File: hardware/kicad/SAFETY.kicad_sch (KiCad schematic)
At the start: 0 parts

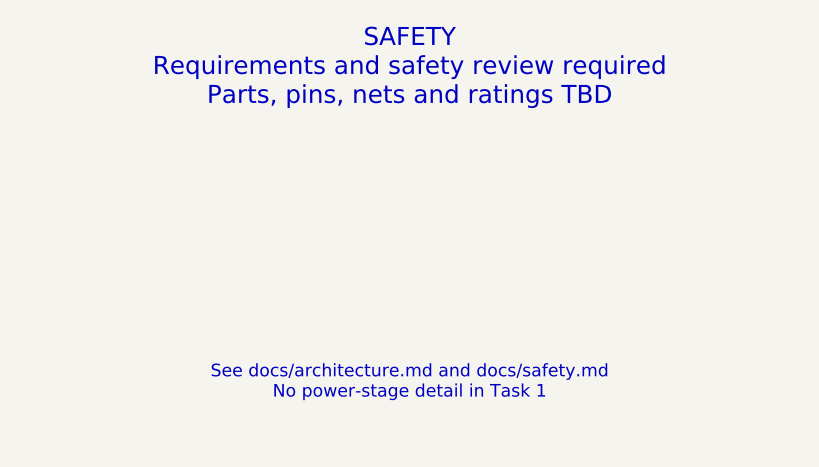
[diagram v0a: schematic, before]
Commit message: hardware: update existing KiCad architecture and add precharge sheet
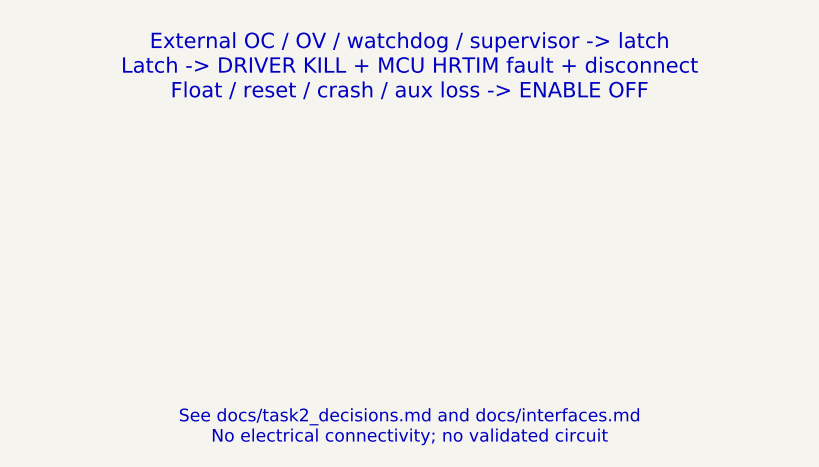
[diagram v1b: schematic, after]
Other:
- note added: "External OC / OV / watchdog / supervisor -> latch Latch -> DRIVER KILL + MCU HRTIM fault + disconnect Float / reset / crash / aux loss -> ENABLE OFF"
- note added: "See docs/task2_decisions.md and docs/interfaces.md No electrical connectivity; no validated circuit"
- note removed: "SAFETY Requirements and safety review required Parts, pins, nets and ratings TBD"
- note removed: "See docs/architecture.md and docs/safety.md No power-stage detail in Task 1"
- title: SAFETY - Placeholder -> SAFETY - Task 2 Proposal

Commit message: hardware: implement prototype Rev A electrical schematic
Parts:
- added C100, C101, C102, C103, C104, C105, C106, C107, C108, C109, C110, C111, C115, C116, C117, C118, C119, C120, C82, C83, C84, C85, C86, C87, C88, C89, C90, C91, C92, C93, C94, C95, C96, C97, C98, C99: 100nF / 16V X7R, Capacitor_SMD:C_0805_2012Metric, symbol RevA:C
- added C112, C113, C114: 1nF /50V, Capacitor_SMD:C_0805_2012Metric, symbol RevA:C
- added J21: latched fault diagnostic output, Connector_PinHeader_2.54mm:PinHeader_1x02_P2.54mm_Vertical, symbol RevA:J2
- added R164: 58.7k /1%, Resistor_SMD:R_0805_2012Metric, symbol RevA:R
- added R165, R167: 10k /PROVISIONAL, Resistor_SMD:R_0805_2012Metric, symbol RevA:R
- added R166: 29.4k /1%, Resistor_SMD:R_0805_2012Metric, symbol RevA:R
- added R168: 29.4k, Resistor_SMD:R_0805_2012Metric, symbol RevA:R
- added R169: 10k / IL14A PROVISIONAL, Resistor_SMD:R_0805_2012Metric, symbol RevA:R
- added R170, R172, R173, R174, R175, R176, R177, R178, R179, R180, R182, R184, R187, R196, R198: 10k, Resistor_SMD:R_0805_2012Metric, symbol RevA:R
- added R171: 10k / preset timeout; verify SET1 table, Resistor_SMD:R_0805_2012Metric, symbol RevA:R
- added R181, R183: 1.74k /PROVISIONAL, Resistor_SMD:R_0805_2012Metric, symbol RevA:R
- added R185: 3.01k /PROVISIONAL, Resistor_SMD:R_0805_2012Metric, symbol RevA:R
- added R186: 1k, Resistor_SMD:R_0805_2012Metric, symbol RevA:R
- added R188: 2.2k, Resistor_SMD:R_0805_2012Metric, symbol RevA:R
- added R189: 221k /1%, Resistor_SMD:R_0805_2012Metric, symbol RevA:R
- added R190, R192, R194: 10k /1%, Resistor_SMD:R_0805_2012Metric, symbol RevA:R
- added R191: 154k /1%, Resistor_SMD:R_0805_2012Metric, symbol RevA:R
- added R193: 172k /1%, Resistor_SMD:R_0805_2012Metric, symbol RevA:R
- added R195: 80.6k, Resistor_SMD:R_0805_2012Metric, symbol RevA:R
- added R197: 100k, Resistor_SMD:R_0805_2012Metric, symbol RevA:R
- added U28, U29, U32, U50, U52, U54, U59, U60, U63: TLV3202DGKR, Package_SO:VSSOP-8_3x3mm_P0.65mm, symbol RevA:TLV3202DGKR
- added U30, U31, U33, U34, U37, U38, U39, U40, U42, U43, U44, U45, U46, U47, U48, U49, U51, U53, U55, U56, U57, U61, U62, U64: SN74LVC2G08DCUR, Package_SO:VSSOP-8_2.3x2mm_P0.5mm, symbol RevA:SN74LVC2G08DCUR
- added U35: TPS3839K33DBZR, Package_TO_SOT_SMD:SOT-23, symbol RevA:TPS3839K33DBZR
- added U36: TPS3431SDRBR, Package_SON:VSON-8-1EP_3x3mm_P0.65mm_EP1.65x2.4mm, symbol RevA:TPS3431SDRBR
- added U41: SN74LVC1G74DCUR, Package_SO:VSSOP-8_2.3x2mm_P0.5mm, symbol RevA:SN74LVC1G74DCUR
- added U58: TLV431AIDBZR, Package_TO_SOT_SMD:SOT-23, symbol RevA:TLV431AIDBZR
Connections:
- new net ALL_PROTECT_OK: U62.7 (Y1), U64.5 (A2)
- new net ARM_PULSE: U41.1 (CLK)
- new net AUX_OK: U33.3 (Y2), U34.5 (A2)
- new net BANK_OV_DIV: C114.1 (A), R193.2 (B), R194.1 (A), U60.2 (INM1)
- new net BANK_OV_OK: U60.1 (OUT1), U61.6 (B2)
- new net BANK_P_RAW: R193.1 (A)
- new net BANK_TEMP_HI_OK: U54.7 (OUT2), U55.2 (B1)
- new net BANK_TEMP_LO_OK: U54.1 (OUT1), U55.1 (A1)
- new net BANK_THERM_OK: U55.7 (Y1), U56.6 (B2)
- new net BASE_OK: U38.3 (Y2), U39.1 (A1)
- new net BUS_FAST_NEG: U28.6 (INM2)
- new net BUS_FAST_POS: U28.2 (INM1)
- new net BUS_FUSED: R189.1 (A), R191.1 (A)
- new net BUS_ISO_DRIVE: U44.7 (Y1)
- new net BUS_ISO_REQUEST: R174.1 (A), U44.1 (A1)
- new net BUS_LIMIT: R164.2 (B), R165.1 (A), U28.3 (INP1), U28.5 (INP2)
- new net BUS_NEG_OK: U28.7 (OUT2), U30.2 (B1)
- new net BUS_OC_OK: U30.7 (Y1), U31.1 (A1)
- new net BUS_OV_DIV: C112.1 (A), R189.2 (B), R190.1 (A), U59.2 (INM1)
- new net BUS_OV_OK: U59.1 (OUT1), U61.1 (A1)
- new net BUS_POS_OK: U28.1 (OUT1), U30.1 (A1)
- new net BUS_UV_DIV: C113.1 (A), R191.2 (B), R192.1 (A), U59.5 (INP2)
- new net BUS_UV_OK: U59.7 (OUT2), U61.2 (B1)
- new net BUS_WINDOW_OK: U61.5 (A2), U61.7 (Y1)
- new net BYP_BUS_DRIVE: U47.7 (Y1)
- new net BYP_BUS_REQUEST: R177.1 (A), U47.1 (A1)
- new net BYP_CAP_DRIVE: U49.7 (Y1)
- new net BYP_CAP_REQUEST: R179.1 (A), U49.1 (A1)
- new net CAP_FAST_NEG: U29.6 (INM2)
- new net CAP_FAST_POS: U29.2 (INM1)
- new net CAP_ISO_DRIVE: U45.7 (Y1)
- new net CAP_ISO_REQUEST: R175.1 (A), U45.1 (A1)
- new net CAP_LIMIT: R166.2 (B), R167.1 (A), U29.3 (INP1), U29.5 (INP2)
- new net CAP_NEG_OK: U29.7 (OUT2), U30.6 (B2)
- new net CAP_OC_OK: U30.3 (Y2), U31.2 (B1)
- new net CAP_POS_OK: U29.1 (OUT1), U30.5 (A2)
- new net CELLS_HW_OK: U37.7 (Y1), U38.1 (A1)
- new net CELLS_OK: U38.7 (Y1), U39.2 (B1)
- new net CONTACT_PERMIT: U43.7 (Y1), U44.2 (B1), U45.2 (B1), U46.2 (B1), U47.2 (B1), U48.2 (B1), U49.2 (B1)
- new net DRIVER_OV_DIV: R197.2 (B), R198.1 (A), U63.6 (INM2)
- new net DRIVER_OV_OK: U63.7 (OUT2), U64.2 (B1)
- new net DRIVER_PROTECT_OK: U39.5 (A2), U64.3 (Y2)
- new net DRIVER_UV_DIV: R195.2 (B), R196.1 (A), U63.3 (INP1)
- new net DRIVER_UV_OK: U63.1 (OUT1), U64.1 (A1)
- new net DRIVER_WINDOW_OK: U64.6 (B2), U64.7 (Y1)
- new net DUMP_DRIVE: U57.3 (Y2)
- new net DUMP_REQUEST: U57.5 (A2)
- new net FAST_OK: U37.3 (Y2), U38.5 (A2)
- new net FAULT_CLEAR_N: U39.3 (Y2), U40.1 (A1), U42.2 (B1), U42.5 (A2), U43.2 (B1)
- new net FAULT_LATCH_Q: R172.1 (A), U40.6 (B2), U41.5 (Q), U43.1 (A1)
- new net FAULT_LATCH_QN: J21.1 (P1), U41.3 (QN)
- new net FET_TEMP_HI_OK: U50.7 (OUT2), U51.2 (B1)
- new net FET_TEMP_LO_OK: U50.1 (OUT1), U51.1 (A1)
- new net FET_THERM_OK: U51.7 (Y1), U56.1 (A1)
- new net GATE_PERMIT: R173.1 (A), U42.7 (Y1)
- new net GND: C100.2 (B), C101.2 (B), C102.2 (B), C103.2 (B), C104.2 (B), C105.2 (B), C106.2 (B), C107.2 (B), C108.2 (B), C109.2 (B), C110.2 (B), C111.2 (B), C112.2 (B), C113.2 (B), C114.2 (B), C115.2 (B), C116.2 (B), C117.2 (B), C118.2 (B), C119.2 (B), C120.2 (B), C82.2 (B), C83.2 (B), C84.2 (B), C85.2 (B), C86.2 (B), C87.2 (B), C88.2 (B), C89.2 (B), C90.2 (B), C91.2 (B), C92.2 (B), C93.2 (B), C94.2 (B), C95.2 (B), C96.2 (B), C97.2 (B), C98.2 (B), C99.2 (B), J21.2 (P2), R165.2 (B), R167.2 (B), R169.2 (B), R172.2 (B), R173.2 (B), R174.2 (B), R175.2 (B), R176.2 (B), R177.2 (B), R178.2 (B), R179.2 (B), R181.2 (B), R183.2 (B), R185.2 (B), R187.2 (B), R190.2 (B), R192.2 (B), R194.2 (B), R196.2 (B), R198.2 (B), U28.4 (GND), U29.4 (GND), U30.4 (GND), U31.4 (GND), U31.5 (A2), U31.6 (B2), U32.4 (GND), U33.4 (GND), U34.4 (GND), U35.1 (GND), U36.4 (GND), U36.9 (EP), U37.4 (GND), U38.4 (GND), U39.4 (GND), U40.4 (GND), U41.4 (GND), U42.4 (GND), U43.4 (GND), U43.5 (A2), U43.6 (B2), U44.4 (GND), U44.5 (A2), U44.6 (B2), U45.4 (GND), U45.5 (A2), U45.6 (B2), U46.4 (GND), U46.5 (A2), U46.6 (B2), U47.4 (GND), U47.5 (A2), U47.6 (B2), U48.4 (GND), U48.5 (A2), U48.6 (B2), U49.4 (GND), U49.5 (A2), U49.6 (B2), U50.4 (GND), U51.4 (GND), U51.5 (A2), U51.6 (B2), U52.4 (GND), U53.4 (GND), U53.5 (A2), U53.6 (B2), U54.4 (GND), U55.4 (GND), U55.5 (A2), U55.6 (B2), U56.4 (GND), U57.4 (GND), U58.3 (A), U59.4 (GND), U60.4 (GND), U60.5 (INP2), U61.4 (GND), U62.4 (GND), U62.5 (A2), U62.6 (B2), U63.4 (GND), U64.4 (GND)
- new net HW_FAULT_N: U42.3 (Y2)
- new net HW_REF_1V24: R188.2 (B), U58.1 (REF), U58.2 (K), U59.3 (INP1), U59.6 (INM2), U60.3 (INP1), U63.2 (INM1), U63.5 (INP2)
- new net IL_FAST_NEG: U32.6 (INM2)
- new net IL_FAST_POS: U32.2 (INM1)
- new net IL_LIMIT: R168.2 (B), R169.1 (A), U32.3 (INP1), U32.5 (INP2)
- new net IL_NEG_OK: U32.7 (OUT2), U33.2 (B1)
- new net IL_OK: U33.7 (Y1), U34.1 (A1)
- new net IL_POS_OK: U32.1 (OUT1), U33.1 (A1)
- new net LATCH_CLEAR_N: U40.7 (Y1), U41.6 (CLR_N)
- new net L_TEMP_HI_OK: U52.7 (OUT2), U53.2 (B1)
- new net L_TEMP_LO_OK: U52.1 (OUT1), U53.1 (A1)
- new net L_THERM_OK: U53.7 (Y1), U56.2 (B1)
- new net MCU_GATE_REQUEST: U40.5 (A2)
- new net MON_CONFIG_VALID: U38.2 (B1)
- new net MON_DCHG: U37.1 (A1)
- new net MON_DDSG: U37.2 (B1)
- new net NRST: U40.2 (B1)
- new net OC_OK: U34.7 (Y1), U37.5 (A2)
- new net PG_DRV: U33.5 (A2)
- new net PG_MCU: U33.6 (B2)
- new net PORT_OC_N: U31.7 (Y1), U34.2 (B1)
- new net POWER_OK: U34.3 (Y2), U37.6 (B2)
- new net POWER_THERM_OK: U56.5 (A2), U56.7 (Y1)
- new net PRE_BUS_DRIVE: U46.7 (Y1)
- new net PRE_BUS_REQUEST: R176.1 (A), U46.1 (A1)
- new net PRE_CAP_DRIVE: U48.7 (Y1)
- new net PRE_CAP_REQUEST: R178.1 (A), U48.1 (A1)
- new net PROTECT_OK: U39.7 (Y1), U57.1 (A1)
- new net RAILS_WINDOW_OK: U61.3 (Y2), U62.2 (B1)
- new net RAIL_OK: U34.6 (B2), U35.2 (RESET_N)
- new net REFEREE_PERMIT: U39.6 (B2)
- new net REQUEST_PERMIT: U40.3 (Y2), U42.1 (A1)
- new net TEMP_BANK_FILTER: U54.3 (INP1), U54.6 (INM2)
- new net TEMP_BANK_LIMIT: R184.2 (B), R185.1 (A), U54.2 (INM1)
- new net TEMP_FET_FILTER: U50.3 (INP1), U50.6 (INM2)
- new net TEMP_FET_LIMIT: R180.2 (B), R181.1 (A), U50.2 (INM1)
- new net TEMP_L_FILTER: U52.3 (INP1), U52.6 (INM2)
- new net TEMP_L_LIMIT: R182.2 (B), R183.1 (A), U52.2 (INM1)
- new net TEMP_OPEN_LIMIT: R186.2 (B), R187.1 (A), U50.5 (INP2), U52.5 (INP2), U54.5 (INP2)
- new net THERM_OK: U56.3 (Y2), U57.2 (B1), U57.6 (B2)
- new net THERM_PROTECT_OK: U57.7 (Y1), U62.1 (A1)
- new net V12_DRIVER: R195.1 (A), R197.1 (A)
- new net V3V3: C100.1 (A), C101.1 (A), C102.1 (A), C103.1 (A), C104.1 (A), C105.1 (A), C106.1 (A), C107.1 (A), C108.1 (A), C109.1 (A), C110.1 (A), C111.1 (A), C115.1 (A), C116.1 (A), C117.1 (A), C118.1 (A), C119.1 (A), C120.1 (A), C82.1 (A), C83.1 (A), C84.1 (A), C85.1 (A), C86.1 (A), C87.1 (A), C88.1 (A), C89.1 (A), C90.1 (A), C91.1 (A), C92.1 (A), C93.1 (A), C94.1 (A), C95.1 (A), C96.1 (A), C97.1 (A), C98.1 (A), C99.1 (A), R164.1 (A), R166.1 (A), R168.1 (A), R170.2 (B), R171.2 (B), R180.1 (A), R182.1 (A), R184.1 (A), R186.1 (A), R188.1 (A), U28.8 (VCC), U29.8 (VCC), U30.8 (VCC), U31.8 (VCC), U32.8 (VCC), U33.8 (VCC), U34.8 (VCC), U35.3 (VDD), U36.1 (VDD), U36.3 (EN), U36.5 (SET1), U37.8 (VCC), U38.8 (VCC), U39.8 (VCC), U40.8 (VCC), U41.2 (D), U41.7 (PRE_N), U41.8 (VCC), U42.6 (B2), U42.8 (VCC), U43.8 (VCC), U44.8 (VCC), U45.8 (VCC), U46.8 (VCC), U47.8 (VCC), U48.8 (VCC), U49.8 (VCC), U50.8 (VCC), U51.8 (VCC), U52.8 (VCC), U53.8 (VCC), U54.8 (VCC), U55.8 (VCC), U56.8 (VCC), U57.8 (VCC), U59.8 (VCC), U60.6 (INM2), U60.8 (VCC), U61.8 (VCC), U62.8 (VCC), U63.8 (VCC), U64.8 (VCC)
- new net WATCHDOG_OK: R170.1 (A), U36.7 (WDO_N), U38.6 (B2)
- new net WD_CWD: R171.1 (A), U36.2 (CWD)
- new net WD_HEARTBEAT: U36.6 (WDI)
- no-connect marks 0 -> 14
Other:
- note added: "External contacts release slower than gate kill; coil current/release/fuse coordination require separate review."
- note added: "Hardware cell permission requires BQ provisioning; missing/invalid commissioning inhibits startup."
- note added: "Independent IL INA293 + comparator -> async latch clear -> PWM AND + EN LOW, plus HRTIM FLT1."
- note added: "Port INA293 pairs + TLV3202 windows + AND. No ADC polling in OC path; maximum delay unverified."
- note added: "Thermal comparator hot/short/open window; source supply/shared sensor/common shunt failures remain in FMEA."
- note removed: "External OC / OV / watchdog / supervisor -> latch Latch -> DRIVER KILL + MCU HRTIM fault + disconnect Float / reset / crash / aux loss -> ENABLE OFF"
- note removed: "See docs/task2_decisions.md and docs/interfaces.md No electrical connectivity; no validated circuit"
- title: SAFETY - Task 2 Proposal -> SAFETY / Prototype Rev A draft

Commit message: hardware: refine Rev A protection and passive selections
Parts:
- removed C82, C83, C84, C85, C86, C87, C88, C89, C90, C91, C92, C93, C94, C95, C96, C97, C98, C99: 100nF / 16V X7R, Capacitor_SMD:C_0805_2012Metric, symbol RevA:C
- removed J21: latched fault diagnostic output, Connector_PinHeader_2.54mm:PinHeader_1x02_P2.54mm_Vertical, symbol RevA:J2
- removed R164: 58.7k /1%, Resistor_SMD:R_0805_2012Metric, symbol RevA:R
- removed R165, R167: 10k /PROVISIONAL, Resistor_SMD:R_0805_2012Metric, symbol RevA:R
- removed R166: 29.4k /1%, Resistor_SMD:R_0805_2012Metric, symbol RevA:R
- removed R168: 29.4k, Resistor_SMD:R_0805_2012Metric, symbol RevA:R
- removed R169: 10k / IL14A PROVISIONAL, Resistor_SMD:R_0805_2012Metric, symbol RevA:R
- removed U28, U29, U32: TLV3202DGKR, Package_SO:VSSOP-8_3x3mm_P0.65mm, symbol RevA:TLV3202DGKR
- removed U30, U31, U33: SN74LVC2G08DCUR, Package_SO:VSSOP-8_2.3x2mm_P0.5mm, symbol RevA:SN74LVC2G08DCUR
- added C121, C122, C123, C124, C125, C126, C127, C128, C129, C133, C134, C135, C136, C137, C138, C139, C140: 100nF / 16V X7R, Capacitor_SMD:C_0805_2012Metric, symbol RevA:C
- added C130, C131, C132: 1nF /50V, Capacitor_SMD:C_0805_2012Metric, symbol RevA:C
- added J18: latched fault diagnostic output, Connector_PinHeader_2.54mm:PinHeader_1x02_P2.54mm_Vertical, symbol RevA:J2
- added R199: 172k /1%, Resistor_SMD:R_0805_2012Metric, symbol RevA:R
- added R200: 10k /1%, Resistor_SMD:R_0805_2012Metric, symbol RevA:R
- added R201: 80.6k, Resistor_SMD:R_0805_2012Metric, symbol RevA:R
- added R202, R204, R206, R208: 10k, Resistor_SMD:R_0805_2012Metric, symbol RevA:R
- added R203, R207: 100k, Resistor_SMD:R_0805_2012Metric, symbol RevA:R
- added R205: 78.7k, Resistor_SMD:R_0805_2012Metric, symbol RevA:R
- added U65, U66, U69, U71: TLV3202DGKR, Package_SO:VSSOP-8_3x3mm_P0.65mm, symbol RevA:TLV3202DGKR
- added U67, U68, U70, U72: SN74LVC2G08DCUR, Package_SO:VSSOP-8_2.3x2mm_P0.5mm, symbol RevA:SN74LVC2G08DCUR
- C100, C101, C102, C103, C104, C105, C106, C107, C108, C109, C110, C111, C115, C116, C117, C118, C119, C120: MPN (none) -> C0805C104K5RACTU
- C112, C113, C114: value 1nF /50V -> 100nF / 16V X7R; MPN (none) -> C0805C104K5RACTU
- R170: value 10k -> 58.7k /1%; MPN (none) -> CRCW080558K7FKEA
- R171: value 10k / preset timeout; verify SET1 table -> 10k /PROVISIONAL; MPN (none) -> CRCW080510K0FKEA
- R172: value 10k -> 35.7k /1%; MPN (none) -> CRCW080535K7FKEA
- R173: value 10k -> 10k /PROVISIONAL; MPN (none) -> CRCW080510K0FKEA
- R174: value 10k -> 35.7k; MPN (none) -> CRCW080535K7FKEA
- R175: value 10k -> 10k / IL12.035A PROVISIONAL; MPN (none) -> CRCW080510K0FKEA
- R176, R178, R179, R180, R182, R184: MPN (none) -> CRCW080510K0FKEA
- R177: value 10k -> 10k / preset timeout; verify SET1 table; MPN (none) -> CRCW080510K0FKEA
- R181, R183: value 1.74k /PROVISIONAL -> 10k; MPN (none) -> CRCW080510K0FKEA
- R185: value 3.01k /PROVISIONAL -> 10k; MPN (none) -> CRCW080510K0FKEA
- R186: value 1k -> 10k; MPN (none) -> CRCW080510K0FKEA
- R187: value 10k -> 1.74k /PROVISIONAL; MPN (none) -> CRCW08051K74FKEA
- R188: value 2.2k -> 10k; MPN (none) -> CRCW080510K0FKEA
- R189: value 221k /1% -> 1.74k /PROVISIONAL; MPN (none) -> CRCW08051K74FKEA
- R190: value 10k /1% -> 10k; MPN (none) -> CRCW080510K0FKEA
- R191: value 154k /1% -> 3.01k /PROVISIONAL; MPN (none) -> CRCW08053K01FKEA
- R192: value 10k /1% -> 1k; MPN (none) -> CRCW08051K00FKEA
- R193: value 172k /1% -> 10k; MPN (none) -> CRCW080510K0FKEA
- R194: value 10k /1% -> 2.2k; MPN (none) -> CRCW08052K20FKEA
- R195: value 80.6k -> 221k /1%; MPN (none) -> CRCW0805221KFKEA
- R196, R198: value 10k -> 10k /1%; MPN (none) -> CRCW080510K0FKEA
- R197: value 100k -> 154k /1%; MPN (none) -> CRCW0805154KFKEA
- U34, U38, U56: value SN74LVC2G08DCUR -> TLV3202DGKR; footprint Package_SO:VSSOP-8_2.3x2mm_P0.5mm -> Package_SO:VSSOP-8_3x3mm_P0.65mm; symbol RevA:SN74LVC2G08DCUR -> RevA:TLV3202DGKR; MPN (none) -> TLV3202DGKR
- U35: value TPS3839K33DBZR -> TLV3202DGKR; footprint Package_TO_SOT_SMD:SOT-23 -> Package_SO:VSSOP-8_3x3mm_P0.65mm; symbol RevA:TPS3839K33DBZR -> RevA:TLV3202DGKR; MPN (none) -> TLV3202DGKR
- U36: value TPS3431SDRBR -> SN74LVC2G08DCUR; footprint Package_SON:VSON-8-1EP_3x3mm_P0.65mm_EP1.65x2.4mm -> Package_SO:VSSOP-8_2.3x2mm_P0.5mm; symbol RevA:TPS3431SDRBR -> RevA:SN74LVC2G08DCUR; MPN (none) -> SN74LVC2G08DCUR
- U37, U39, U40, U43, U44, U45, U46, U48, U49, U51, U53, U55, U57, U61, U62: MPN (none) -> SN74LVC2G08DCUR
- U41: value SN74LVC1G74DCUR -> TPS3839K33DBZR; footprint Package_SO:VSSOP-8_2.3x2mm_P0.5mm -> Package_TO_SOT_SMD:SOT-23; symbol RevA:SN74LVC1G74DCUR -> RevA:TPS3839K33DBZR; MPN (none) -> TPS3839K33DBZR
- U42: value SN74LVC2G08DCUR -> TPS3431SDRBR; footprint Package_SO:VSSOP-8_2.3x2mm_P0.5mm -> Package_SON:VSON-8-1EP_3x3mm_P0.65mm_EP1.65x2.4mm; symbol RevA:SN74LVC2G08DCUR -> RevA:TPS3431SDRBR; MPN (none) -> TPS3431SDRBR
- U47: value SN74LVC2G08DCUR -> SN74LVC1G74DCUR; symbol RevA:SN74LVC2G08DCUR -> RevA:SN74LVC1G74DCUR; MPN (none) -> SN74LVC1G74DCUR
- U50, U52, U54, U59, U63: value TLV3202DGKR -> SN74LVC2G08DCUR; footprint Package_SO:VSSOP-8_3x3mm_P0.65mm -> Package_SO:VSSOP-8_2.3x2mm_P0.5mm; symbol RevA:TLV3202DGKR -> RevA:SN74LVC2G08DCUR; MPN (none) -> SN74LVC2G08DCUR
- U58: value TLV431AIDBZR -> TLV3202DGKR; footprint Package_TO_SOT_SMD:SOT-23 -> Package_SO:VSSOP-8_3x3mm_P0.65mm; symbol RevA:TLV431AIDBZR -> RevA:TLV3202DGKR; MPN (none) -> TLV3202DGKR
- U60: MPN (none) -> TLV3202DGKR
- U64: value SN74LVC2G08DCUR -> TLV431AIDBZR; footprint Package_SO:VSSOP-8_2.3x2mm_P0.5mm -> Package_TO_SOT_SMD:SOT-23; symbol RevA:SN74LVC2G08DCUR -> RevA:TLV431AIDBZR; MPN (none) -> TLV431AIDBZR
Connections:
- net ALL_PROTECT_OK: now also U68.7 (Y1), U70.5 (A2); no longer U62.7 (Y1), U64.5 (A2)
- net ARM_PULSE: now also U47.1 (CLK); no longer U41.1 (CLK)
- net AUX_OK: now also U39.3 (Y2), U40.5 (A2); no longer U34.5 (A2)
- net BANK_OV_DIV: now also C132.1 (A), R199.2 (B), R200.1 (A), U66.2 (INM1); no longer C114.1 (A), R193.2 (B), R194.1 (A), U60.2 (INM1)
- net BANK_OV_OK: now also U66.1 (OUT1), U67.6 (B2); no longer U60.1 (OUT1), U61.6 (B2)
- net BANK_P_RAW: now also R199.1 (A); no longer R193.1 (A)
- net BANK_TEMP_HI_OK: now also U60.7 (OUT2), U61.2 (B1); no longer U54.7 (OUT2), U55.2 (B1)
- net BANK_TEMP_LO_OK: now also U60.1 (OUT1), U61.1 (A1); no longer U54.1 (OUT1), U55.1 (A1)
- net BANK_THERM_OK: now also U61.7 (Y1), U62.6 (B2); no longer U55.7 (Y1), U56.6 (B2)
- net BASE_OK: now also U44.3 (Y2), U45.1 (A1); no longer U38.3 (Y2), U39.1 (A1)
- net BUS_FAST_NEG: now also U34.6 (INM2)
- net BUS_FAST_POS: now also U34.2 (INM1)
- net BUS_FUSED: now also R195.1 (A), R197.1 (A); no longer R189.1 (A), R191.1 (A)
- net BUS_ISO_DRIVE: now also U50.7 (Y1); no longer U44.7 (Y1)
- net BUS_ISO_REQUEST: now also R180.1 (A), U50.1 (A1); no longer R174.1 (A), U44.1 (A1)
- net BUS_LIMIT: now also R170.2 (B), R171.1 (A), U34.3 (INP1), U34.5 (INP2)
- net BUS_NEG_OK: now also U34.7 (OUT2), U36.2 (B1)
- net BUS_OC_OK: now also U36.7 (Y1), U37.1 (A1)
- net BUS_OV_DIV: now also R195.2 (B), R196.1 (A), C130.1 (A), U65.2 (INM1); no longer C112.1 (A), R189.2 (B), R190.1 (A), U59.2 (INM1)
- net BUS_OV_OK: now also U65.1 (OUT1), U67.1 (A1); no longer U59.1 (OUT1), U61.1 (A1)
- net BUS_POS_OK: now also U34.1 (OUT1), U36.1 (A1)
- net BUS_UV_DIV: now also R197.2 (B), R198.1 (A), C131.1 (A), U65.5 (INP2); no longer C113.1 (A), R191.2 (B), R192.1 (A), U59.5 (INP2)
- net BUS_UV_OK: now also U65.7 (OUT2), U67.2 (B1); no longer U59.7 (OUT2), U61.2 (B1)
- net BUS_WINDOW_OK: now also U67.5 (A2), U67.7 (Y1); no longer U61.5 (A2), U61.7 (Y1)
- net BYP_BUS_DRIVE: now also U53.7 (Y1); no longer U47.7 (Y1)
- net BYP_BUS_REQUEST: now also R183.1 (A), U53.1 (A1); no longer R177.1 (A), U47.1 (A1)
- net BYP_CAP_DRIVE: now also U55.7 (Y1); no longer U49.7 (Y1)
- net BYP_CAP_REQUEST: now also R185.1 (A), U55.1 (A1); no longer R179.1 (A), U49.1 (A1)
- net CAP_FAST_NEG: now also U35.6 (INM2)
- net CAP_FAST_POS: now also U35.2 (INM1)
- net CAP_ISO_DRIVE: now also U51.7 (Y1); no longer U45.7 (Y1)
- net CAP_ISO_REQUEST: now also R181.1 (A), U51.1 (A1); no longer R175.1 (A), U45.1 (A1)
- net CAP_LIMIT: now also R172.2 (B), R173.1 (A), U35.3 (INP1), U35.5 (INP2)
- net CAP_NEG_OK: now also U35.7 (OUT2), U36.6 (B2)
- net CAP_OC_OK: now also U36.3 (Y2), U37.2 (B1)
- net CAP_POS_OK: now also U35.1 (OUT1), U36.5 (A2)
- net CELLS_HW_OK: now also U43.7 (Y1), U44.1 (A1); no longer U37.7 (Y1), U38.1 (A1)
- net CELLS_OK: now also U44.7 (Y1), U45.2 (B1); no longer U38.7 (Y1), U39.2 (B1)
- net CONTACT_PERMIT: now also U49.7 (Y1), U50.2 (B1), U51.2 (B1), U52.2 (B1), U53.2 (B1), U54.2 (B1), U55.2 (B1); no longer U43.7 (Y1), U44.2 (B1), U45.2 (B1), U46.2 (B1), U47.2 (B1), U48.2 (B1), U49.2 (B1)
- net DRIVER_OV_DIV: now also R203.2 (B), R204.1 (A), U69.6 (INM2); no longer R197.2 (B), R198.1 (A), U63.6 (INM2)
- net DRIVER_OV_OK: now also U69.7 (OUT2), U70.2 (B1); no longer U63.7 (OUT2), U64.2 (B1)
- net DRIVER_PROTECT_OK: now also U70.3 (Y2), U72.5 (A2); no longer U39.5 (A2), U64.3 (Y2)
- net DRIVER_UV_DIV: now also R201.2 (B), R202.1 (A), U69.3 (INP1); no longer R195.2 (B), R196.1 (A), U63.3 (INP1)
- net DRIVER_UV_OK: now also U69.1 (OUT1), U70.1 (A1); no longer U63.1 (OUT1), U64.1 (A1)
- net DRIVER_WINDOW_OK: now also U70.6 (B2), U70.7 (Y1); no longer U64.6 (B2), U64.7 (Y1)
- net DUMP_DRIVE: now also U63.3 (Y2); no longer U57.3 (Y2)
- net DUMP_REQUEST: now also U63.5 (A2); no longer U57.5 (A2)
- net FAST_OK: now also U43.3 (Y2), U44.5 (A2); no longer U37.3 (Y2), U38.5 (A2)
- net FAULT_CLEAR_N: now also U45.3 (Y2), U46.1 (A1), U48.2 (B1), U48.5 (A2), U49.2 (B1); no longer U39.3 (Y2), U40.1 (A1), U42.2 (B1), U42.5 (A2), U43.2 (B1)
- net FAULT_LATCH_Q: now also R178.1 (A), U46.6 (B2), U47.5 (Q), U49.1 (A1); no longer R172.1 (A), U40.6 (B2), U41.5 (Q), U43.1 (A1)
- net FAULT_LATCH_QN: now also U47.3 (QN), J18.1 (P1); no longer U41.3 (QN)
- net FET_TEMP_HI_OK: now also U56.7 (OUT2), U57.2 (B1); no longer U50.7 (OUT2), U51.2 (B1)
- net FET_TEMP_LO_OK: now also U56.1 (OUT1), U57.1 (A1); no longer U50.1 (OUT1), U51.1 (A1)
- net FET_THERM_OK: now also U57.7 (Y1), U62.1 (A1); no longer U51.7 (Y1), U56.1 (A1)
- net GATE_PERMIT: now also R179.1 (A), U48.7 (Y1); no longer R173.1 (A), U42.7 (Y1)
- net GND: now also R171.2 (B), R180.2 (B), R182.2 (B), R184.2 (B), R189.2 (B), R191.2 (B), R193.2 (B), U35.4 (GND), U37.5 (A2), U37.6 (B2), U41.1 (GND), U42.9 (EP), U50.5 (A2), U50.6 (B2), U52.5 (A2), U52.6 (B2), U54.5 (A2), U54.6 (B2), U57.5 (A2), U57.6 (B2), U58.4 (GND), U59.5 (A2), U59.6 (B2), U61.5 (A2), U61.6 (B2), U64.3 (A), C121.2 (B), C122.2 (B), C123.2 (B), C124.2 (B), C125.2 (B), C126.2 (B), C127.2 (B), C128.2 (B), C129.2 (B), C130.2 (B), C131.2 (B), C132.2 (B), C133.2 (B), C134.2 (B), C135.2 (B), C136.2 (B), C137.2 (B), C138.2 (B), C139.2 (B), C140.2 (B), J18.2 (P2), R200.2 (B), R202.2 (B), R204.2 (B), R206.2 (B), R208.2 (B), U65.4 (GND), U66.4 (GND), U66.5 (INP2), U67.4 (GND), U68.4 (GND), U68.5 (A2), U68.6 (B2), U69.4 (GND), U70.4 (GND), U71.4 (GND), U72.4 (GND); no longer R172.2 (B), R174.2 (B), R176.2 (B), R177.2 (B), R190.2 (B), R192.2 (B), R194.2 (B), U35.1 (GND), U36.9 (EP), U41.4 (GND), U43.5 (A2), U43.6 (B2), U44.5 (A2), U44.6 (B2), U45.5 (A2), U45.6 (B2), U46.5 (A2), U46.6 (B2), U47.5 (A2), U47.6 (B2), U48.5 (A2), U48.6 (B2), U58.3 (A), U60.5 (INP2), U62.5 (A2), U62.6 (B2), U64.4 (GND)
- net HW_FAULT_N: now also U48.3 (Y2); no longer U42.3 (Y2)
- net HW_REF_1V24: now also R194.2 (B), U64.1 (REF), U64.2 (K), U65.3 (INP1), U65.6 (INM2), U66.3 (INP1), U69.2 (INM1), U69.5 (INP2), U71.2 (INM1), U71.5 (INP2); no longer R188.2 (B), U58.1 (REF), U58.2 (K), U59.3 (INP1), U59.6 (INM2), U60.3 (INP1), U63.2 (INM1), U63.5 (INP2)
- net IL_FAST_NEG: now also U38.6 (INM2)
- net IL_FAST_POS: now also U38.2 (INM1)
- net IL_LIMIT: now also R174.2 (B), R175.1 (A), U38.3 (INP1), U38.5 (INP2)
- net IL_NEG_OK: now also U38.7 (OUT2), U39.2 (B1)
- net IL_OK: now also U39.7 (Y1), U40.1 (A1); no longer U34.1 (A1)
- net IL_POS_OK: now also U38.1 (OUT1), U39.1 (A1)
- net LATCH_CLEAR_N: now also U46.7 (Y1), U47.6 (CLR_N); no longer U40.7 (Y1), U41.6 (CLR_N)
- net L_TEMP_HI_OK: now also U58.7 (OUT2), U59.2 (B1); no longer U52.7 (OUT2), U53.2 (B1)
- net L_TEMP_LO_OK: now also U58.1 (OUT1), U59.1 (A1); no longer U52.1 (OUT1), U53.1 (A1)
- net L_THERM_OK: now also U59.7 (Y1), U62.2 (B1); no longer U53.7 (Y1), U56.2 (B1)
- net MCU_GATE_REQUEST: now also U46.5 (A2); no longer U40.5 (A2)
- net MON_CONFIG_VALID: now also U44.2 (B1); no longer U38.2 (B1)
- net MON_DCHG: now also U43.1 (A1); no longer U37.1 (A1)
- net MON_DDSG: now also U43.2 (B1); no longer U37.2 (B1)
- net NRST: now also U46.2 (B1); no longer U40.2 (B1)
- net OC_OK: now also U40.7 (Y1), U43.5 (A2); no longer U34.7 (Y1), U37.5 (A2)
- net PG_DRV: now also U39.5 (A2)
- net PG_MCU: now also U39.6 (B2)
- net PORT_OC_N: now also U37.7 (Y1), U40.2 (B1); no longer U34.2 (B1)
- net POWER_OK: now also U40.3 (Y2), U43.6 (B2); no longer U34.3 (Y2), U37.6 (B2)
- net POWER_THERM_OK: now also U62.5 (A2), U62.7 (Y1); no longer U56.5 (A2), U56.7 (Y1)
- net PRE_BUS_DRIVE: now also U52.7 (Y1); no longer U46.7 (Y1)
- net PRE_BUS_REQUEST: now also R182.1 (A), U52.1 (A1); no longer R176.1 (A), U46.1 (A1)
- net PRE_CAP_DRIVE: now also U54.7 (Y1); no longer U48.7 (Y1)
- net PRE_CAP_REQUEST: now also R184.1 (A), U54.1 (A1); no longer R178.1 (A), U48.1 (A1)
- net PROTECT_OK: now also U45.7 (Y1), U63.1 (A1); no longer U39.7 (Y1), U57.1 (A1)
- net RAILS_WINDOW_OK: now also U67.3 (Y2), U68.2 (B1); no longer U61.3 (Y2), U62.2 (B1)
- net RAIL_OK: now also U40.6 (B2), U41.2 (RESET_N); no longer U34.6 (B2), U35.2 (RESET_N)
- net REFEREE_PERMIT: now also U45.6 (B2); no longer U39.6 (B2)
- net REQUEST_PERMIT: now also U46.3 (Y2), U48.1 (A1); no longer U40.3 (Y2), U42.1 (A1)
- net TEMP_BANK_FILTER: now also U60.3 (INP1), U60.6 (INM2); no longer U54.3 (INP1), U54.6 (INM2)
- net TEMP_BANK_LIMIT: now also R190.2 (B), R191.1 (A), U60.2 (INM1); no longer R184.2 (B), R185.1 (A), U54.2 (INM1)
- net TEMP_FET_FILTER: now also U56.3 (INP1), U56.6 (INM2); no longer U50.3 (INP1), U50.6 (INM2)
- net TEMP_FET_LIMIT: now also R186.2 (B), R187.1 (A), U56.2 (INM1); no longer R180.2 (B), R181.1 (A), U50.2 (INM1)
- net TEMP_L_FILTER: now also U58.3 (INP1), U58.6 (INM2); no longer U52.3 (INP1), U52.6 (INM2)
- net TEMP_L_LIMIT: now also R188.2 (B), R189.1 (A), U58.2 (INM1); no longer R182.2 (B), R183.1 (A), U52.2 (INM1)
- net TEMP_OPEN_LIMIT: now also R192.2 (B), R193.1 (A), U56.5 (INP2), U58.5 (INP2), U60.5 (INP2); no longer R186.2 (B), R187.1 (A), U50.5 (INP2), U52.5 (INP2), U54.5 (INP2)
- net THERM_OK: now also U62.3 (Y2), U63.2 (B1), U63.6 (B2); no longer U56.3 (Y2), U57.2 (B1), U57.6 (B2)
- net THERM_PROTECT_OK: now also U63.7 (Y1), U68.1 (A1); no longer U57.7 (Y1), U62.1 (A1)
- net V12_DRIVER: now also R201.1 (A), R203.1 (A); no longer R195.1 (A), R197.1 (A)
- net V3V3: now also C112.1 (A), C113.1 (A), C114.1 (A), R170.1 (A), R172.1 (A), R174.1 (A), R176.2 (B), R177.2 (B), R190.1 (A), R192.1 (A), R194.1 (A), U35.8 (VCC), U36.8 (VCC), U41.3 (VDD), U42.1 (VDD), U42.3 (EN), U42.5 (SET1), U47.2 (D), U47.7 (PRE_N), U48.6 (B2), U58.8 (VCC), C121.1 (A), C122.1 (A), C123.1 (A), C124.1 (A), C125.1 (A), C126.1 (A), C127.1 (A), C128.1 (A), C129.1 (A), C133.1 (A), C134.1 (A), C135.1 (A), C136.1 (A), C137.1 (A), C138.1 (A), C139.1 (A), C140.1 (A), U65.8 (VCC), U66.6 (INM2), U66.8 (VCC), U67.8 (VCC), U68.8 (VCC), U69.8 (VCC), U70.8 (VCC), U71.8 (VCC), U72.8 (VCC); no longer R170.2 (B), R171.2 (B), R180.1 (A), R182.1 (A), R184.1 (A), U35.3 (VDD), U36.1 (VDD), U36.3 (EN), U36.5 (SET1), U41.2 (D), U41.7 (PRE_N), U41.8 (VCC), U42.6 (B2), U42.8 (VCC), U60.6 (INM2), U64.8 (VCC)
- net WATCHDOG_OK: now also R176.1 (A), U42.7 (WDO_N), U44.6 (B2); no longer R170.1 (A), U36.7 (WDO_N), U38.6 (B2)
- net WD_CWD: now also R177.1 (A), U42.2 (CWD); no longer R171.1 (A), U36.2 (CWD)
- net WD_HEARTBEAT: now also U42.6 (WDI); no longer U36.6 (WDI)
- new net ACTUATOR_12V: R205.1 (A), R207.1 (A)
- new net ACTUATOR_OV_DIV: R207.2 (B), R208.1 (A), U71.6 (INM2)
- new net ACTUATOR_OV_OK: U71.7 (OUT2), U72.2 (B1)
- new net ACTUATOR_UV_DIV: R205.2 (B), R206.1 (A), U71.3 (INP1)
- new net ACTUATOR_UV_OK: U71.1 (OUT1), U72.1 (A1)
- new net ACTUATOR_WINDOW_OK: U72.6 (B2), U72.7 (Y1)
- new net ASSEMBLY_PROTECT_OK: U45.5 (A2), U72.3 (Y2)
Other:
- moved on the sheet: C100, C101, C102, C103, C104, C105, C106, C107, C108, C109, C110, C111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
